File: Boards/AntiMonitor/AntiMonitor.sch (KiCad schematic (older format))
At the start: 17 parts, among them J1 Data Bus, J2 Address Bus, J3 PWR, J4 System Bus, SW1 SW_SPDT, SW2 RESET, U1 74LS299, U2 74LS299, U3 74LS299

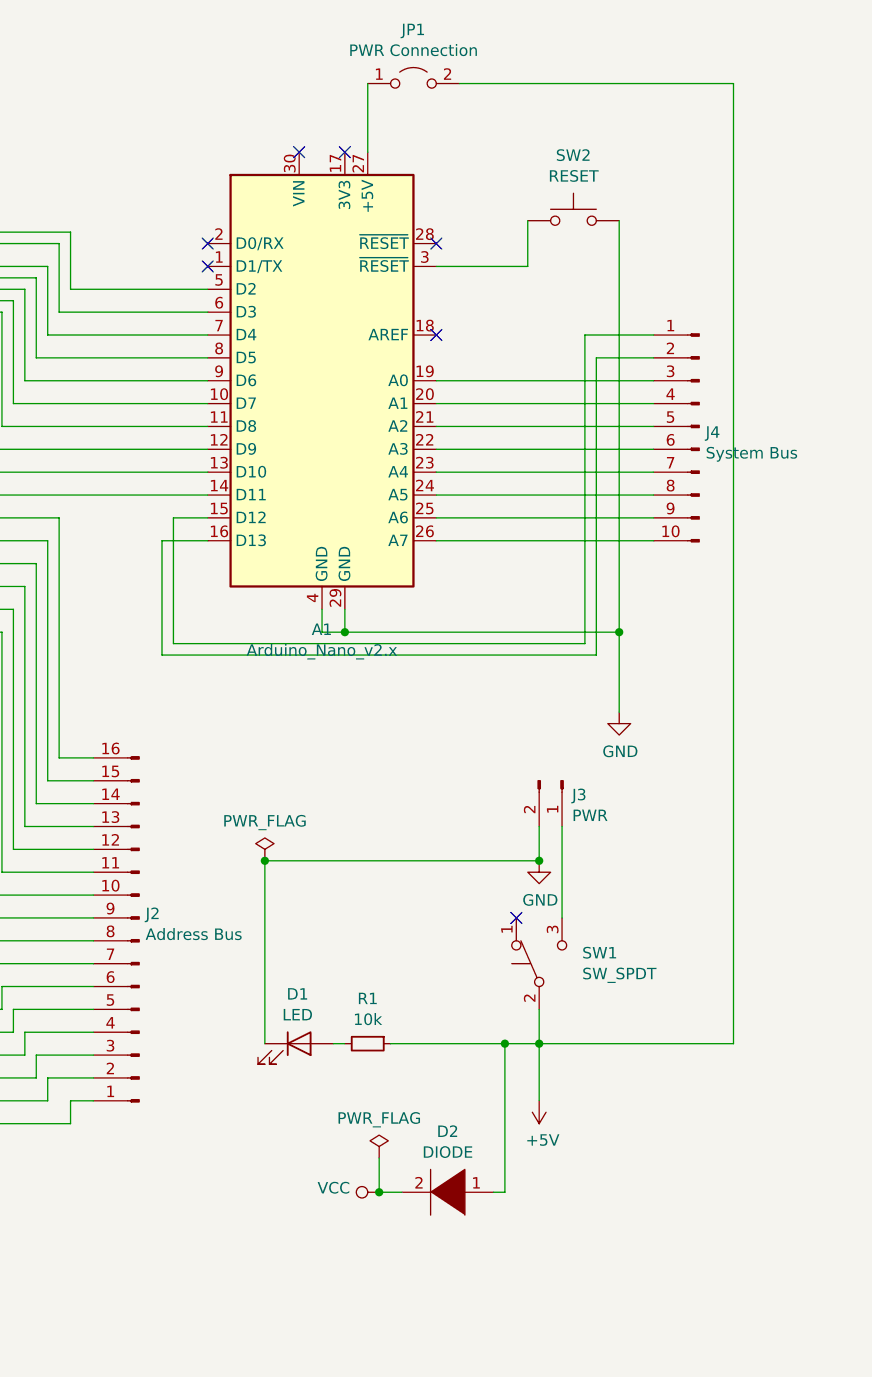
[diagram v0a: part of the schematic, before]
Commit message: * Antimonitor board update * INT controller tweaks * Opcode XML adjusted slightly * Table builder to output C++ EMU tables * ZASM updates
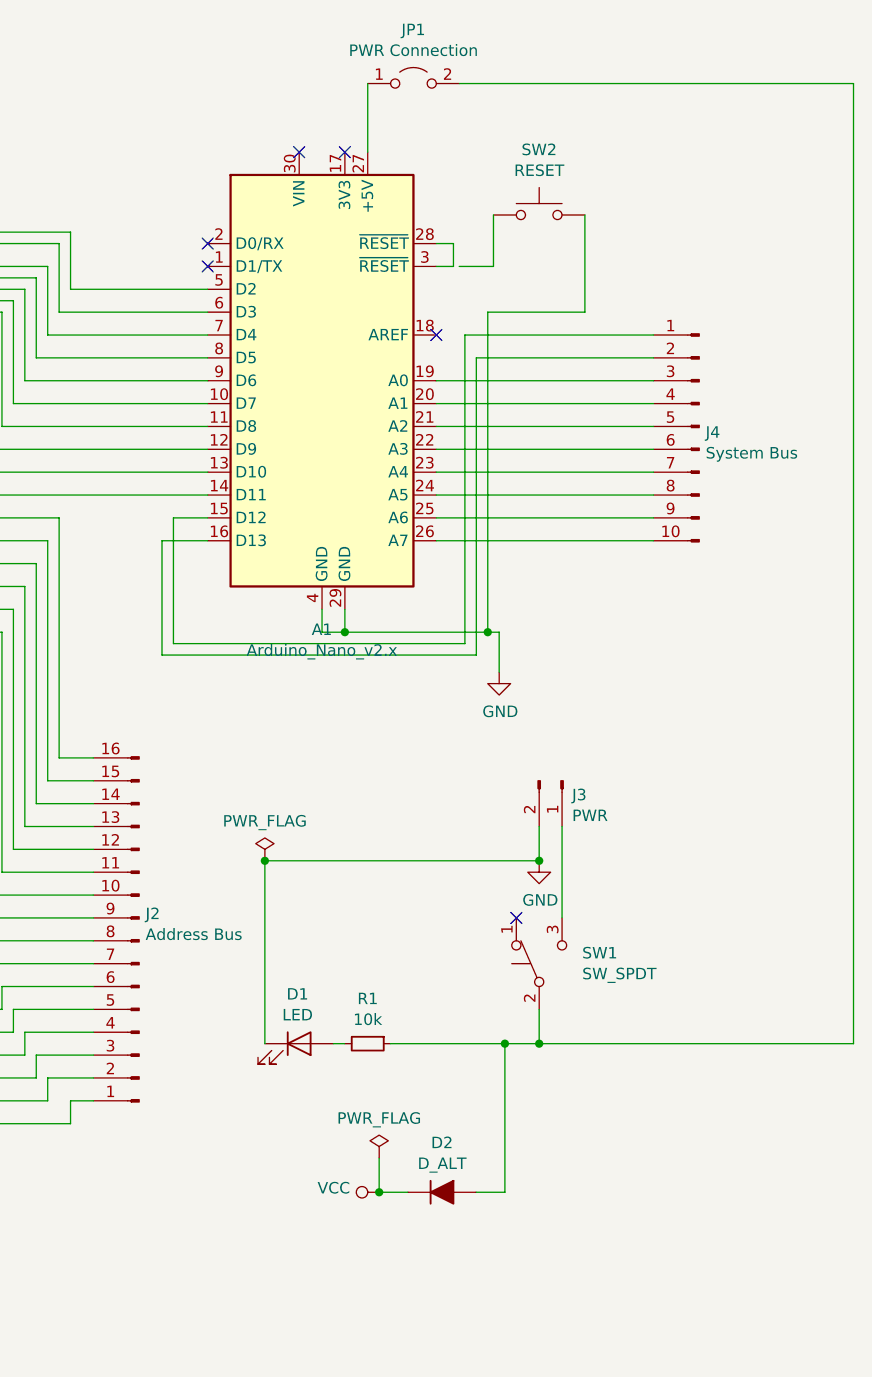
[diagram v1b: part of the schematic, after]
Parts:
- removed D2: DIODE, Diode_THT:D_5W_P12.70mm_Horizontal, symbol pspice:DIODE
- added D2: D_ALT, Diode_THT:D_A-405_P7.62mm_Horizontal, symbol Device:D_ALT
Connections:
- net VCC: now also D2.1 (K)
- net at A1.28 (~RESET): now also A1.3 (~RESET)
- net at SW2.1: no longer A1.3 (~RESET)
- net +5V: no longer names the net of JP1.2 (B), R1.1, SW1.2 (B)
- net +5V: now also D2.2 (A)
- no-connect marks 13 -> 12
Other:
- moved on the sheet: SW2
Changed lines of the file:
@@
 	1    0    0    -1
 $EndComp
-Wire Wire Line
-	9700 1500 9700 1700
-Wire Wire Line
-	9700 1700 9300 1700
 $Comp
 L Switch:SW_Push SW2
 U 1 1 5E30E722
-P 9900 1500
-F 0 "SW2" H 9900 1785 50  0000 C CNN
-F 1 "RESET" H 9900 1694 50  0000 C CNN
-F 2 "Button_Switch_THT:SW_PUSH_6mm_H5mm" H 9900 1700 50  0001 C CNN
-F 3 "~" H 9900 1700 50  0001 C CNN
-	1    9900 1500
+P 9750 1475
+F 0 "SW2" H 9750 1760 50  0000 C CNN
+F 1 "RESET" H 9750 1669 50  0000 C CNN
+F 2 "Button_Switch_THT:SW_PUSH_6mm_H5mm" H 9750 1675 50  0001 C CNN
+F 3 "~" H 9750 1675 50  0001 C CNN
+	1    9750 1475
 	1    0    0    -1
 $EndComp
@@
 L power:GND #PWR05
 U 1 1 5E310B17
-P 10100 3650
-F 0 "#PWR05" H 10100 3400 50  0001 C CNN
-F 1 "GND" H 10105 3477 50  0000 C CNN
-F 2 "" H 10100 3650 50  0001 C CNN
-F 3 "" H 10100 3650 50  0001 C CNN
-	1    10100 3650
+P 9575 3475
+F 0 "#PWR05" H 9575 3225 50  0001 C CNN
+F 1 "GND" H 9580 3302 50  0000 C CNN
+F 2 "" H 9575 3475 50  0001 C CNN
+F 3 "" H 9575 3475 50  0001 C CNN
+	1    9575 3475
 	1    0    0    -1
 $EndComp
 NoConn ~ 9300 2000
-NoConn ~ 9300 1600
 Wire Wire Line
 	8900 3200 8900 3300
 Wire Wire Line
-	8900 3300 10100 3300
-Wire Wire Line
-	10100 1500 10100 3300
+	8900 3300 9525 3300
 Wire Wire Line
 	8800 3200 8800 3300
@@
 Connection ~ 8900 3300
 Wire Wire Line
-	10100 3300 10100 3650
-Connection ~ 10100 3300
-Wire Wire Line
-	9300 2900 10250 2900
-Wire Wire Line
-	10250 2800 9300 2800
-Wire Wire Line
-	9300 2700 10250 2700
-Wire Wire Line
-	10250 2600 9300 2600
-Wire Wire Line
-	9300 2500 10250 2500
-Wire Wire Line
-	10250 2400 9300 2400
-Wire Wire Line
-	9300 2300 10250 2300
-Wire Wire Line
-	10250 2200 9300 2200
-Wire Wire Line
-	10250 2100 10000 2100
-Wire Wire Line
-	10000 3400 8100 3400
+	9475 3400 8100 3400
 Wire Wire Line
 	8100 3400 8100 2900
@@
 	8100 2900 8300 2900
 Wire Wire Line
-	10250 2000 9950 2000
-Wire Wire Line
-	9950 2000 9950 3350
+	9425 2000 9425 3350
 Wire Wire Line
 	8150 3350 8150 2800
@@
 NoConn ~ 8900 1200
 Wire Wire Line
-	10000 2100 10000 3400
-Wire Wire Line
-	9950 3350 8150 3350
+	9475 2100 9475 3400
+Wire Wire Line
+	9425 3350 8150 3350
 Wire Wire Line
 	9000 900  9000 1200
@@
 	8550 4300 8550 5100
 Connection ~ 9750 4300
-$Comp
-L power:+5V #PWR04
-U 1 1 5E354311
-P 9750 5350
-F 0 "#PWR04" H 9750 5200 50  0001 C CNN
-F 1 "+5V" H 9765 5523 50  0000 C CNN
-F 2 "" H 9750 5350 50  0001 C CNN
-F 3 "" H 9750 5350 50  0001 C CNN
-	1    9750 5350
-	1    0    0    1
-$EndComp
 Wire Wire Line
 	9750 4950 9750 5100
@@
 NoConn ~ 2550 3350
 Wire Wire Line
-	9400 900  10600 900
-Wire Wire Line
-	10600 900  10600 5100
+	9400 900  11125 900
+Wire Wire Line
+	11125 900  11125 5100
 NoConn ~ 9650 4550
 Wire Wire Line
@@
 Wire Wire Line
 	4600 4100 4600 4650
-Wire Wire Line
-	9750 5100 9750 5350
 Wire Wire Line
 	4700 3850 4700 4300
@@
 $EndComp
 Wire Wire Line
-	9750 5100 10600 5100
+	9750 5100 11125 5100
 Wire Wire Line
 	9100 5100 9600 5100
-Wire Wire Line
-	9150 5750 9050 5750
 Wire Wire Line
 	9050 5750 9050 5600
 NoConn ~ 8300 1700
 NoConn ~ 8300 1600
-$Comp
-L pspice:DIODE D2
-U 1 1 5EC1FAE9
-P 9350 5750
-F 0 "D2" H 9350 5485 50  0000 C CNN
-F 1 "DIODE" H 9350 5576 50  0000 C CNN
-F 2 "Diode_THT:D_5W_P12.70mm_Horizontal" H 9350 5750 50  0001 C CNN
-F 3 "~" H 9350 5750 50  0001 C CNN
-	1    9350 5750
-	-1   0    0    1
-$EndComp
-Wire Wire Line
-	9550 5750 9600 5750
-Wire Wire Line
-	9600 5750 9600 5100
 Connection ~ 9600 5100
 Wire Wire Line
@@
 	-1   0    0    1
 $EndComp
+Wire Wire Line
+	9600 5100 9600 5750
+Wire Wire Line
+	9475 5750 9600 5750
+Wire Wire Line
+	9175 5750 9050 5750
+$Comp
+L Device:D_ALT D2
+U 1 1 5E5FD12E
+P 9325 5750
+F 0 "D2" H 9325 5966 50  0000 C CNN
+F 1 "D_ALT" H 9325 5875 50  0000 C CNN
+F 2 "Diode_THT:D_A-405_P7.62mm_Horizontal" H 9325 5750 50  0001 C CNN
+F 3 "~" H 9325 5750 50  0001 C CNN
+	1    9325 5750
+	1    0    0    -1
+$EndComp
+Wire Wire Line
+	9300 1600 9375 1600
+Wire Wire Line
+	9375 1600 9375 1700
+Wire Wire Line
+	9375 1700 9300 1700
+Wire Wire Line
+	9400 1700 9550 1700
+Wire Wire Line
+	9550 1700 9550 1475
+Wire Wire Line
+	9575 3300 9575 3475
+Wire Wire Line
+	9950 1900 9525 1900
+Wire Wire Line
+	9525 1900 9525 3300
+Wire Wire Line
+	9950 1475 9950 1900
+Connection ~ 9525 3300
+Wire Wire Line
+	9525 3300 9575 3300
+Wire Wire Line
+	9300 2900 10250 2900
+Wire Wire Line
+	9300 2800 10250 2800
+Wire Wire Line
+	9300 2700 10250 2700
+Wire Wire Line
+	9300 2600 10250 2600
+Wire Wire Line
+	9300 2500 10250 2500
+Wire Wire Line
+	9300 2400 10250 2400
+Wire Wire Line
+	9300 2300 10250 2300
+Wire Wire Line
+	9300 2200 10250 2200
+Wire Wire Line
+	9475 2100 10250 2100
+Wire Wire Line
+	9425 2000 10250 2000
 $EndSCHEMATC
